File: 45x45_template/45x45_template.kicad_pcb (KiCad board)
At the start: 2 copper layers, 45 x 45 mm, 12 parts, among them J2 Screw_Terminal_01x02, SW1 SW_Push, SW2 SW_Push

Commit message: New libs.
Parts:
- removed R6: 100k, Resistor_SMD:R_1206_3216Metric_Pad1.30x1.75mm_HandSolder
- removed REF**: ele_petnica_logo, PEP:ele_petnica_logo
- added R2: 100k, Resistor_SMD:R_1206_3216Metric_Pad1.30x1.75mm_HandSolder, F.Cu at (164.0, 88.9)
- added R3: ~, PEP_library:R_Axial_DIN0207_L6.3mm_D2.5mm_P15.24mm_Horizontal, F.Cu at (155.4, 82.0)
- moved R1 34.1 mm to (164.0, 85.6), turned to 0 degrees
- moved SW2 30.1 mm to (152.5, 94.5), turned to 0 degrees
- moved SW1 19.0 mm to (152.5, 86.0), turned to 0 degrees
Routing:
- net Net-(R2-Pad1): track 9.66 -> 0.00 mm
- net (no net): track 0.00 -> 9.66 mm

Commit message: Library updates.
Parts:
- moved R3 78.9 mm to (76.8, 89.0)

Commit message: Templates updated.
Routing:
- removed copper zone on B.Cu, net 0
- removed copper zone on F.Cu, net 0
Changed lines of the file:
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@@
 		)
+	)
+	(gr_arc
+		(start 148.286213 101.041988)
+		(mid 147.022693 104.0924)
+		(end 143.972283 105.355919)
+		(stroke
+			(width 1.4)
+			(type default)
+		)
+		(layer "F.Cu")
+		(net 1)
+	)
+	(gr_line
+		(start 148.272285 101.041989)
+		(end 148.272283 66.041989)
+		(stroke
+			(width 1.4)
+			(type default)
+		)
+		(layer "F.Cu")
+		(net 1)
+	)
+	(gr_arc
+		(start 104.667579 66.019704)
+		(mid 105.921866 62.991572)
+		(end 108.949999 61.737285)
+		(stroke
+			(width 1.4)
+			(type default)
+		)
+		(layer "F.Cu")
+		(net 1)
+	)
+	(gr_line
+		(start 108.972283 105.341989)
+		(end 143.972283 105.341989)
+		(stroke
+			(width 1.4)
+			(type default)
+		)
+		(layer "F.Cu")
+		(net 1)
+	)
+	(gr_line
+		(start 143.750001 61.75)
+		(end 108.749999 61.75)
+		(stroke
+			(width 1.4)
+			(type default)
+		)
+		(layer "F.Cu")
+		(net 1)
+	)
+	(gr_arc
+		(start 108.972283 105.355919)
+		(mid 105.921873 104.092398)
+		(end 104.658353 101.041988)
+		(stroke
+			(width 1.4)
+			(type default)
+		)
+		(layer "F.Cu")
+		(net 1)
+	)
+	(gr_arc
+		(start 143.983329 61.735989)
+		(mid 147.028108 62.99721)
+		(end 148.289329 66.041988)
+		(stroke
+			(width 1.4)
+			(type default)
+		)
+		(layer "F.Cu")
+		(net 1)
+	)
+	(gr_line
+		(start 104.672283 66.041989)
+		(end 104.672283 101.041989)
+		(stroke
+			(width 1.4)
+			(type default)
+		)
+		(layer "F.Cu")
+		(net 1)
+	)
+	(gr_arc
+		(start 148.286213 101.041988)
+		(mid 147.022693 104.0924)
+		(end 143.972283 105.355919)
+		(stroke
+			(width 1.4)
+			(type default)
+		)
+		(layer "B.Cu")
+		(net 1)
+	)
+	(gr_arc
+		(start 104.667579 66.019704)
+		(mid 105.921866 62.991572)
+		(end 108.949999 61.737285)
+		(stroke
+			(width 1.4)
+			(type default)
+		)
+		(layer "B.Cu")
+		(net 1)
+	)
+	(gr_arc
+		(start 108.972283 105.355919)
+		(mid 105.921873 104.092398)
+		(end 104.658353 101.041988)
+		(stroke
+			(width 1.4)
+			(type default)
+		)
+		(layer "B.Cu")
+		(net 1)
+	)
+	(gr_line
+		(start 148.272285 101.041989)
+		(end 148.272283 66.041989)
+		(stroke
+			(width 1.4)
+			(type default)
+		)
+		(layer "B.Cu")
+		(net 1)
+	)
+	(gr_line
+		(start 143.750001 61.75)
+		(end 108.749999 61.75)
+		(stroke
+			(width 1.4)
+			(type default)
+		)
+		(layer "B.Cu")
+		(net 1)
+	)
+	(gr_arc
+		(start 143.983329 61.735989)
+		(mid 147.028108 62.99721)
+		(end 148.289329 66.041988)
+		(stroke
+			(width 1.4)
+			(type default)
+		)
+		(layer "B.Cu")
+		(net 1)
+	)
+	(gr_line
+		(start 104.672283 66.041989)
+		(end 104.672283 101.041989)
+		(stroke
+			(width 1.4)
+			(type default)
+		)
+		(layer "B.Cu")
+		(net 1)
+	)
+	(gr_line
+		(start 108.972283 105.341989)
+		(end 143.972283 105.341989)
+		(stroke
+			(width 1.4)
+			(type default)
+		)
+		(layer "B.Cu")
+		(net 1)
 	)
 	(gr_line
@@
 		(net 5)
 	)
-	(zone
-		(net 1)
-		(net_name "0")
-		(layer "F.Cu")
-		(hatch edge 0.5)
-		(priority 1)
-		(connect_pads
-			(clearance 0.5)
-		)
-		(min_thickness 0.25)
-		(filled_areas_thickness no)
-		(fill yes
-			(thermal_gap 0.5)
-			(thermal_bridge_width 0.5)
-		)
-		(polygon
-			(pts
-				(xy 104 61) (xy 149 61) (xy 149 106) (xy 104 106)
-			)
-		)
-	)
-	(zone
-		(net 1)
-		(net_name "0")
-		(layer "B.Cu")
-		(hatch edge 0.5)
-		(connect_pads
-			(clearance 0.5)
-		)
-		(min_thickness 0.25)
-		(filled_areas_thickness no)
-		(fill yes
-			(thermal_gap 0.5)
-			(thermal_bridge_width 0.5)
-		)
-		(polygon
-			(pts
-				(xy 104 61) (xy 149 61) (xy 149 106) (xy 104 106)
-			)
-		)
-	)
-	(zone
-		(net 1)
-		(net_name "0")
-		(layer "B.Cu")
-		(hatch edge 0.5)
-		(priority 1)
-		(connect_pads
-			(clearance 0.5)
-		)
-		(min_thickness 0.25)
-		(filled_areas_thickness no)
-		(fill yes
-			(thermal_gap 0.5)
-			(thermal_bridge_width 0.5)
-		)
-		(polygon
-			(pts
-				(xy 104 61) (xy 149 61) (xy 149 106) (xy 104 106)
-			)
-		)
-	)
 )

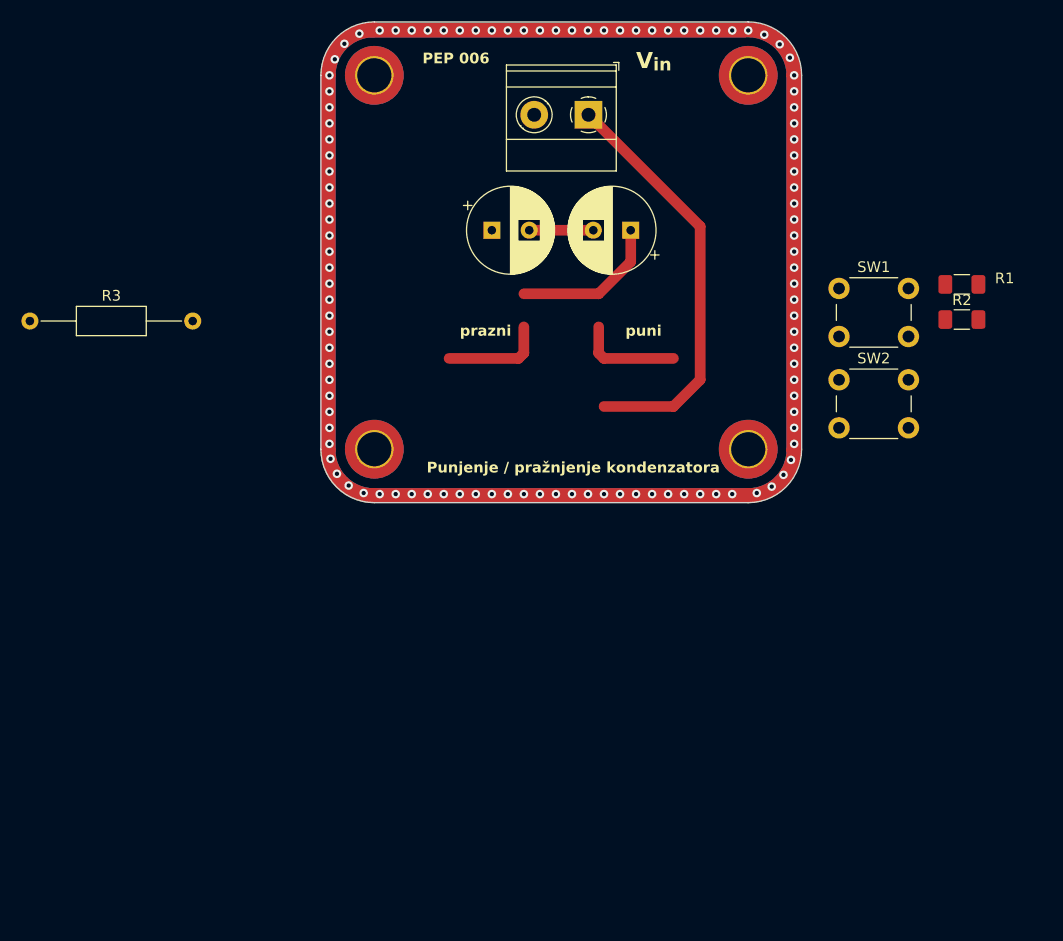
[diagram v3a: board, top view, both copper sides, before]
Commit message: Template, library and PEP7 update.
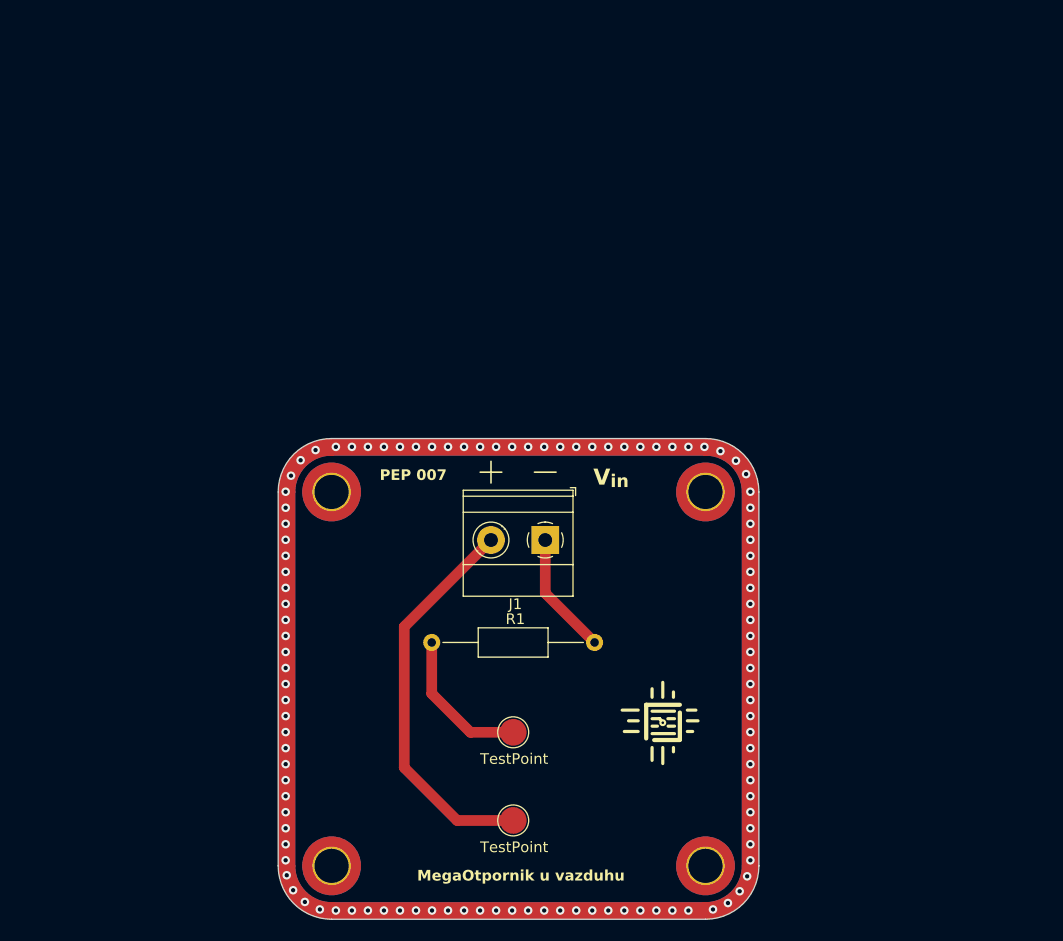
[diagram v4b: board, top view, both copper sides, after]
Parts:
- removed C1, C2: 100u, Capacitor_THT:CP_Radial_D8.0mm_P3.50mm
- removed J2: Screw_Terminal_01x02, TerminalBlock_Phoenix:TerminalBlock_Phoenix_MKDS-1,5-2-5.08_1x02_P5.08mm_Horizontal
- removed R2: 100k, Resistor_SMD:R_1206_3216Metric_Pad1.30x1.75mm_HandSolder
- removed R3: ~, PEP_library:R_Axial_DIN0207_L6.3mm_D2.5mm_P15.24mm_Horizontal
- removed SW1, SW2: SW_Push, Button_Switch_THT:SW_PUSH_6mm_H4.3mm
- added J1: Screw_Terminal_01x02, PEP_library:TerminalBlock_Phoenix_MKDS-1,5-2-5.08_1x02_P5.08mm_Horizontal, F.Cu at (125.0, 109.5)
- added REF**: ele_petnica_logo, PEP_library:ele_petnica_logo, F.Cu at (136.0, 126.6)
- added TP2: TestPoint, TestPoint:TestPoint_Pad_D2.5mm, F.Cu at (122.0, 127.5)
- added TP2: TestPoint, TestPoint:TestPoint_Pad_D2.5mm, F.Cu at (122.0, 135.8)
- R1: value 100k -> 1Meg; footprint Resistor_SMD:R_1206_3216Metric_Pad1.30x1.75mm_HandSolder -> PEP_library:R_Axial_DIN0207_L6.3mm_D2.5mm_P15.24mm_Horizontal
- moved R1 59.9 mm to (114.4, 119.1)
- moved H1 39.2 mm to (105.0, 140.0)
- moved H2 39.2 mm to (105.0, 105.0)
- moved H3 39.2 mm to (140.0, 105.0)
- moved H4 39.2 mm to (140.0, 140.0)
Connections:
- R1 pad 2: Output voltage -> Input voltage
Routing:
- net 0: track 0.00 -> 36.9 mm, vias 109 -> 0
- net Input voltage: track 39.2 -> 11.5 mm
- net Output voltage: track 14.2 -> 0.00 mm
- net (no net): track 9.66 -> 0.00 mm, vias 0 -> 109
- net Net-(C1-Pad2): track 6.00 -> 0.00 mm
- net Net-(R1-Pad1): track 9.66 -> 13.9 mm
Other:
- board text added: "MegaOtpornik u vazduhu"
- board text added: "PEP 007"
- board text added: "TestPoint"
- board text removed: "PEP 006"
- board text removed: "Punjenje / pražnjenje kondenzatora"
- board text removed: "prazni"
- board text removed: "puni"
